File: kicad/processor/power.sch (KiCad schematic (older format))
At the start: 29 parts, among them J201 V_QI, J202 GND, J301 Battery, Q203 DMG3415U, Q204 DMG3415U, Q301 DMG3414U, Q302 DMG3415U, Q303 DMG3415U, U301 MCP73832, U302 NCP694-3.3

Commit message: Restructure directories - separate projects for each board,
separate directory for analysis, datasheets
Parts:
- removed LED301: Charge, paddle:SMD_D_0805, symbol LED3MM
- added LED?: LED, paddle:SMD_D_0805, symbol LED
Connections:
- wire segments 72 -> 96
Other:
- moved on the sheet: D?

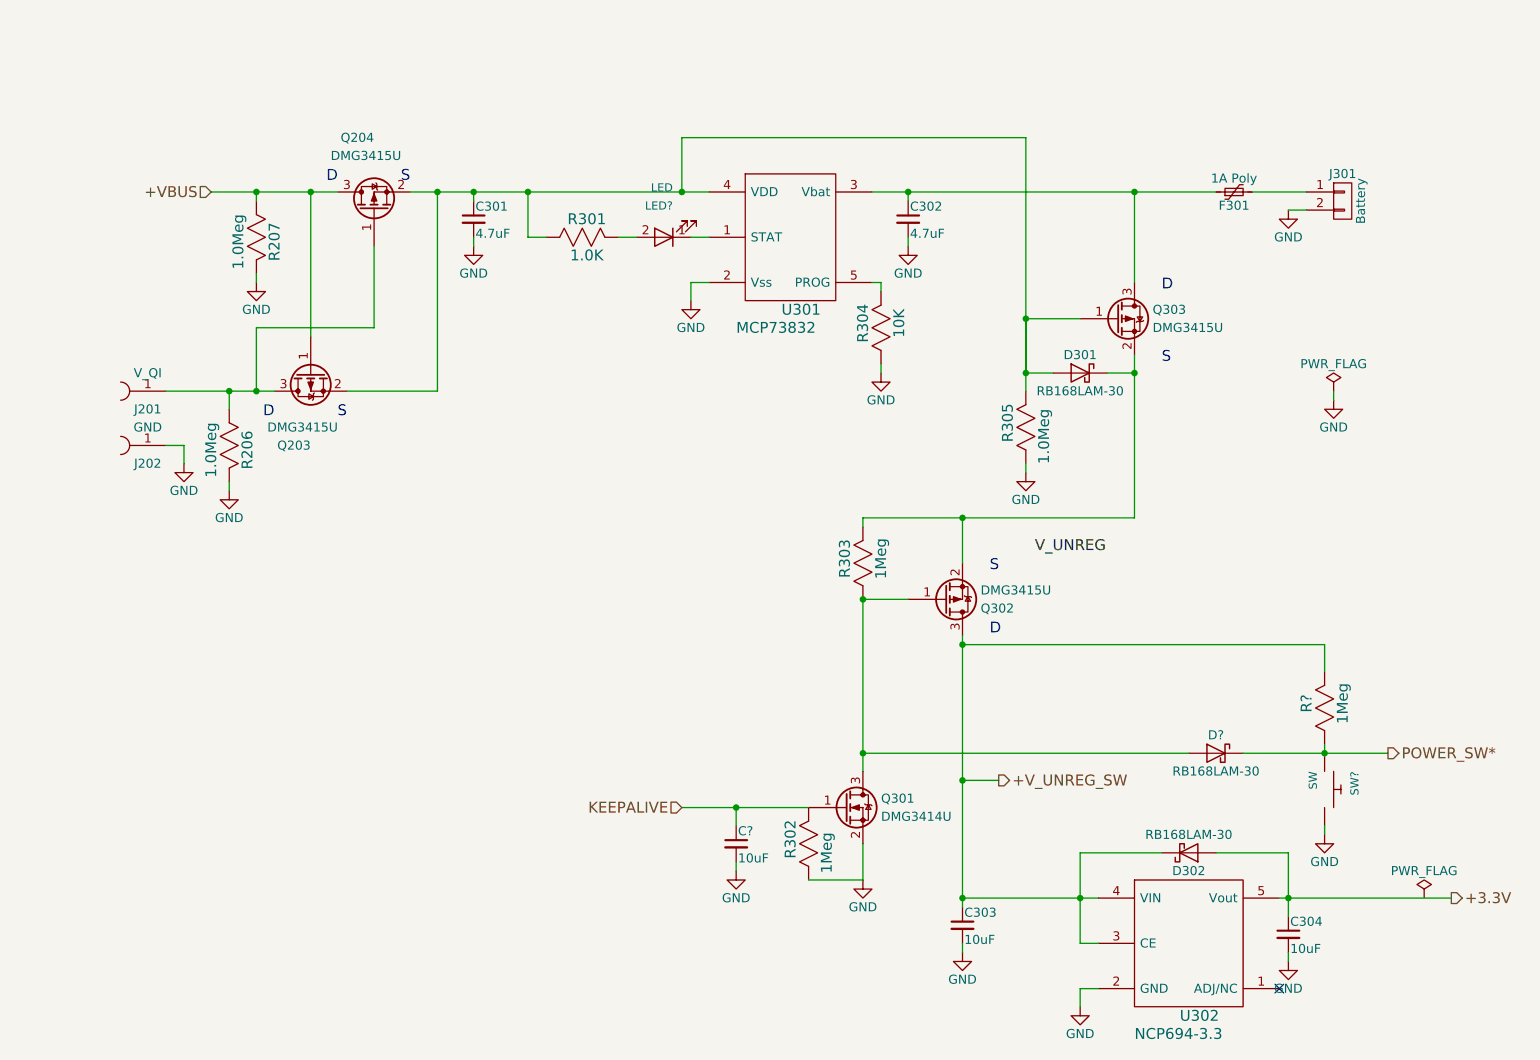
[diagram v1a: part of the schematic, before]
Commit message: Finish split projects, fix ERC, import outline to processor board
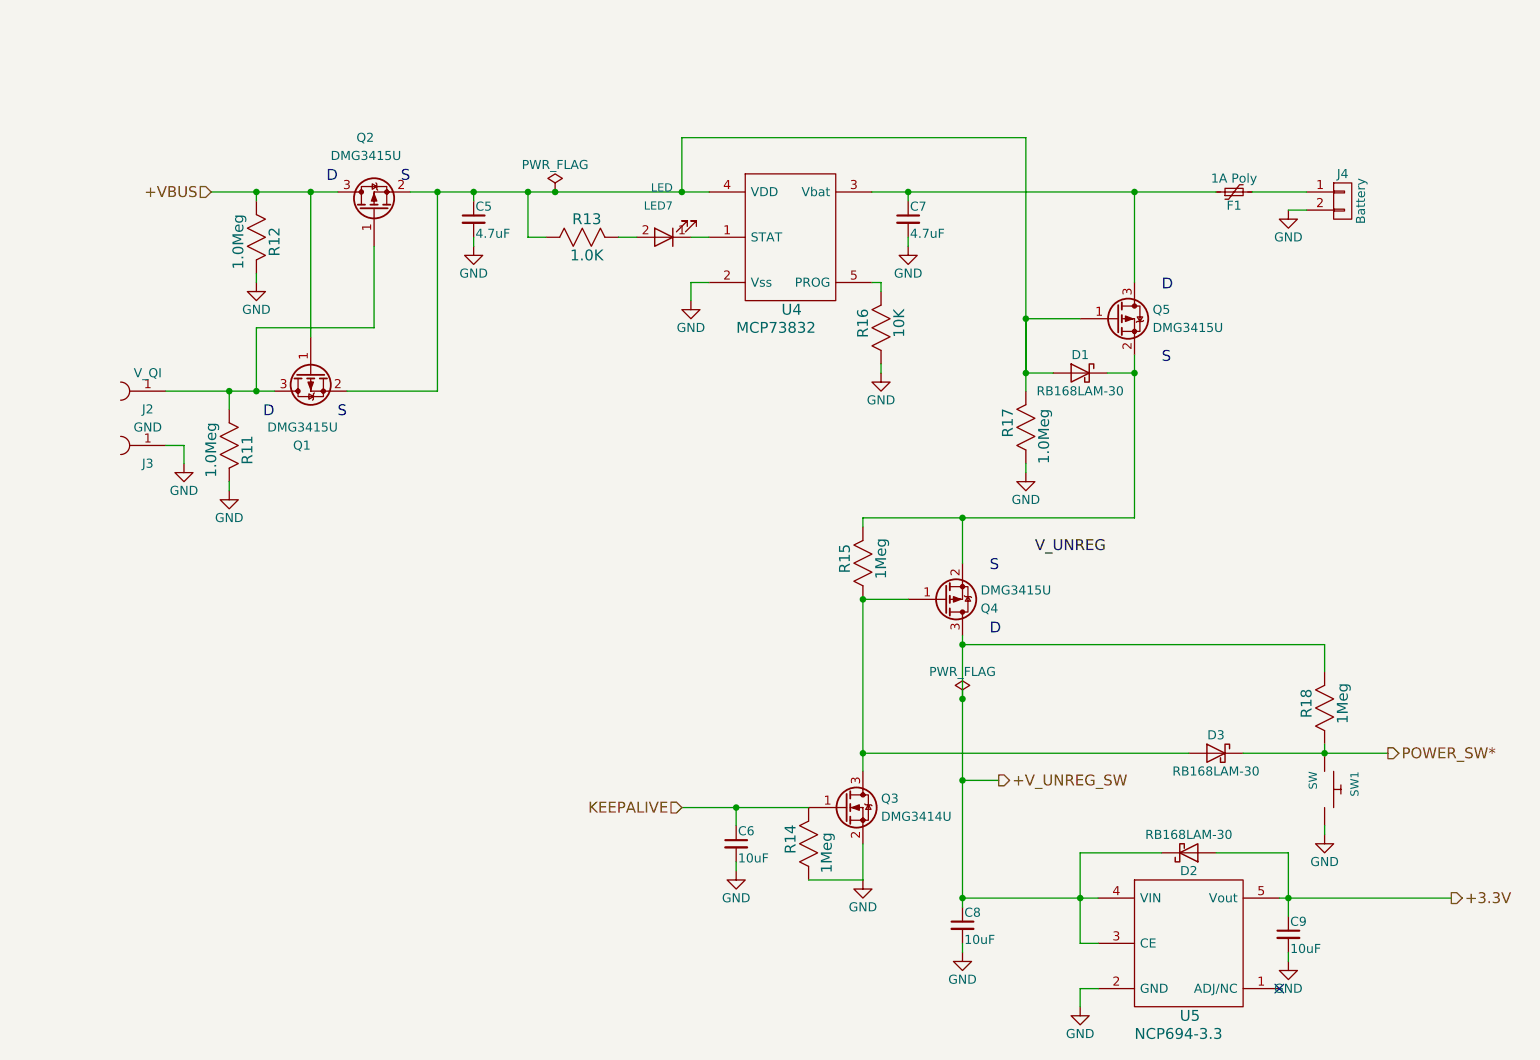
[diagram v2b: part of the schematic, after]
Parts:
- gave numbers to parts that had none: 5
- renumbered C301 to C5, C302 to C7, C303 to C8, C304 to C9, D301 to D1, D302 to D2, F301 to F1, J201 to J2, J202 to J3, J301 to J4, Q203 to Q1, Q204 to Q2, Q301 to Q3, Q302 to Q4, Q303 to Q5, R206 to R11, R207 to R12, R301 to R13, R302 to R14, R303 to R15, R304 to R16, R305 to R17, U301 to U4, U302 to U5

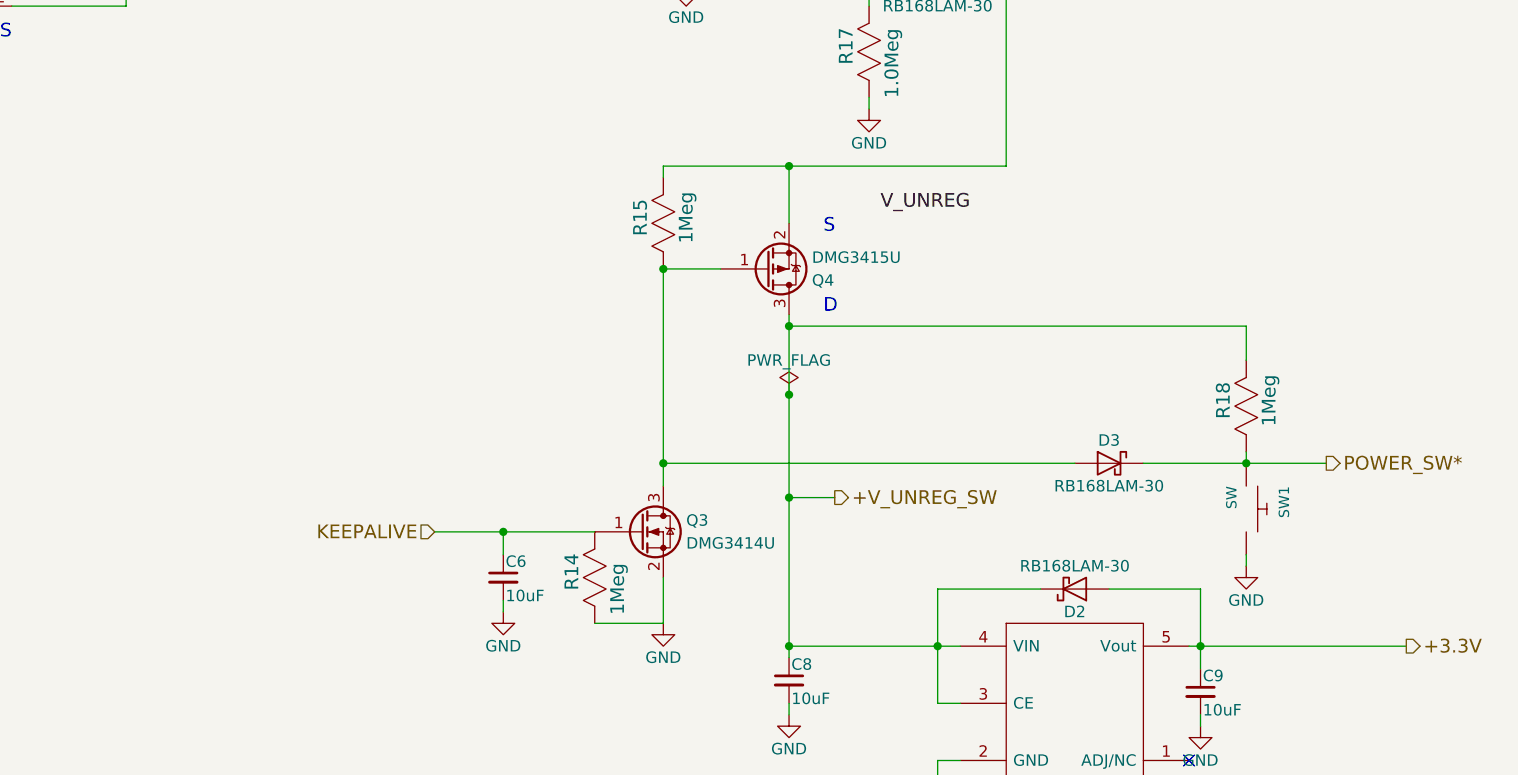
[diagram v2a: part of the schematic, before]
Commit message: Logic board standalone about done, changed to 0603 resistors and 0805 caps
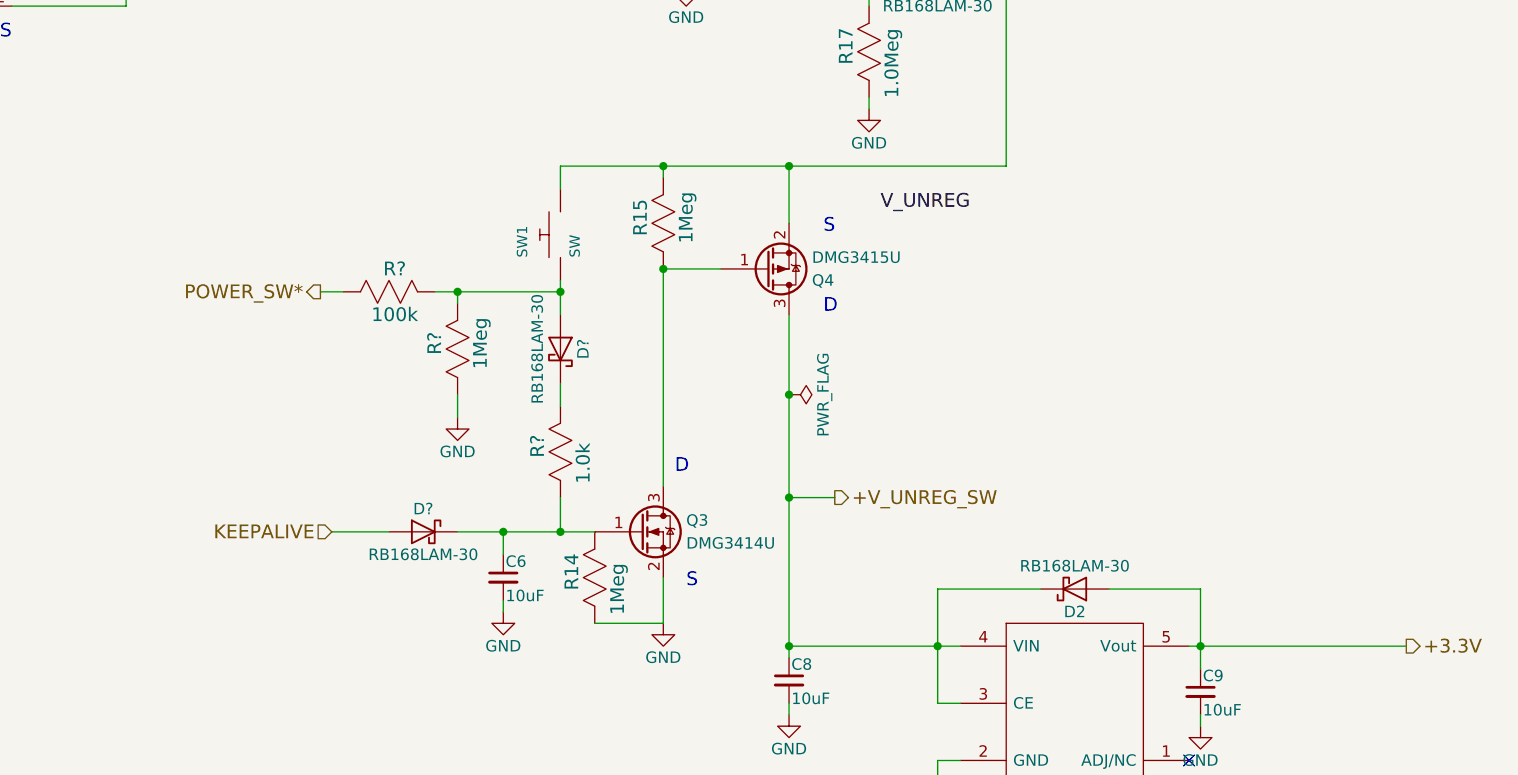
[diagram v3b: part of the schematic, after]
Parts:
- removed D3: RB168LAM-30, paddle:D_SOD-123, symbol Schottky
- removed R18: 1Meg, paddle:SMD_0805, symbol R_US
- added D? (x2): RB168LAM-30, paddle:D_SOD-128, symbol Schottky
- added R?: 1.0k, paddle:R_0603, symbol R_US
- added R?: 1Meg, paddle:R_0603, symbol R_US
- added R?: 100k, paddle:R_0603, symbol R_US
- C5, C6, C7, C8, C9: footprint paddle:SMD_1206 -> paddle:SMD_0805
- D1: footprint paddle:D_SOD-123 -> paddle:D_SOD-128
- R11, R12, R13, R14, R15, R16, R17: footprint paddle:SMD_0805 -> paddle:R_0603
- SW1: footprint paddle:SW_TACTILE_PB_SMD_6MM -> paddle:SW_KMR7
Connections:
- net GND: now also R?.1; no longer SW1.2
- net KEEPALIVE: now also D?.1; no longer C6.1, Q3.1 (G), R14.2
- net POWER_SW*: now also R?.1; no longer SW1.1
- net at D1.2, Q4.2 (S), Q5.2 (S)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: now also SW1.2
- new net: C6.1, D?.2, Q3.1 (G), R14.2, R?.1
- new net: D?.1, R?.2, R?.2, SW1.1
- new net: D?.2, R?.2
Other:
- moved on the sheet: SW1
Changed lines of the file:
@@
 F 0 "C8" H 6710 5970 50  0000 L CNN
 F 1 "10uF" H 6710 5820 50  0000 L CNN
-F 2 "paddle:SMD_1206" H 6700 5900 50  0001 C CNN
+F 2 "paddle:SMD_0805" H 6700 5900 50  0001 C CNN
 F 3 "" H 6700 5900 50  0001 C CNN
 	1    6700 5900
@@
 F 0 "R15" H 6175 4000 60  0000 C CNN
 F 1 "1Meg" H 6175 3800 60  0000 C CNN
-F 2 "paddle:SMD_0805" H 6150 3550 60  0001 C CNN
+F 2 "paddle:R_0603" H 6150 3550 60  0001 C CNN
 F 3 "" H 6175 4000 60  0000 C CNN
 	1    6150 3900
@@
 F 0 "R14" H 5875 5550 60  0000 C CNN
 F 1 "1Meg" H 5800 5350 60  0000 C CNN
-F 2 "paddle:SMD_0805" H 5850 5100 60  0001 C CNN
+F 2 "paddle:R_0603" H 5850 5100 60  0001 C CNN
 F 3 "" H 5875 5550 60  0000 C CNN
 	1    5850 5450
@@
 F 0 "C5" H 4010 2070 50  0000 L CNN
 F 1 "4.7uF" H 4010 1920 50  0000 L CNN
-F 2 "paddle:SMD_1206" H 4000 2000 50  0001 C CNN
+F 2 "paddle:SMD_0805" H 4000 2000 50  0001 C CNN
 F 3 "" H 4000 2000 50  0001 C CNN
 	1    4000 2000
@@
 F 0 "R16" H 6275 2700 60  0000 C CNN
 F 1 "10K" H 6275 2500 60  0000 C CNN
-F 2 "paddle:SMD_0805" H 6250 2250 60  0001 C CNN
+F 2 "paddle:R_0603" H 6250 2250 60  0001 C CNN
 F 3 "" H 6275 2700 60  0000 C CNN
 	1    6250 2600
@@
 	1    0    0    -1
 $EndComp
-Text HLabel 9050 4950 2    60   Output ~ 0
+Text HLabel 4650 4200 0    60   Output ~ 0
 POWER_SW*
-Text HLabel 5150 5250 0    60   Input ~ 0
+Text HLabel 4700 5250 0    60   Input ~ 0
 KEEPALIVE
 $Comp
@@
 F 0 "C7" H 6410 2070 50  0000 L CNN
 F 1 "4.7uF" H 6410 1920 50  0000 L CNN
-F 2 "paddle:SMD_1206" H 6400 2000 50  0001 C CNN
+F 2 "paddle:SMD_0805" H 6400 2000 50  0001 C CNN
 F 3 "" H 6400 2000 50  0001 C CNN
 	1    6400 2000
@@
 F 0 "R13" H 4625 2200 60  0000 C CNN
 F 1 "1.0K" H 4625 2000 60  0000 C CNN
-F 2 "paddle:SMD_0805" H 4600 1750 60  0001 C CNN
+F 2 "paddle:R_0603" H 4600 1750 60  0001 C CNN
 F 3 "" H 4625 2200 60  0000 C CNN
 	1    4600 2100
@@
 F 0 "C9" H 8510 6020 50  0000 L CNN
 F 1 "10uF" H 8510 5870 50  0000 L CNN
-F 2 "paddle:SMD_1206" H 8500 5950 50  0001 C CNN
+F 2 "paddle:SMD_0805" H 8500 5950 50  0001 C CNN
 F 3 "" H 8500 5950 50  0001 C CNN
 	1    8500 5950
@@
 F 0 "R17" H 7075 3250 60  0000 C CNN
 F 1 "1.0Meg" H 7000 3050 60  0000 C CNN
-F 2 "paddle:SMD_0805" H 7050 2800 60  0001 C CNN
+F 2 "paddle:R_0603" H 7050 2800 60  0001 C CNN
 F 3 "" H 7075 3250 60  0000 C CNN
 	1    7050 3150
@@
 F 0 "D1" H 7350 2950 50  0000 C CNN
 F 1 "RB168LAM-30" H 7350 2750 50  0000 C CNN
-F 2 "paddle:D_SOD-123" H 7350 2675 50  0001 C CNN
+F 2 "paddle:D_SOD-128" H 7350 2675 50  0001 C CNN
 F 3 "" H 7350 2850 50  0001 C CNN
 	1    7350 2850
@@
 L GND #PWR039
 U 1 1 59D182BE
-P 8700 5400
-F 0 "#PWR039" H 8700 5150 50  0001 C CNN
-F 1 "GND" H 8700 5250 50  0000 C CNN
-F 2 "" H 8700 5400 50  0001 C CNN
-F 3 "" H 8700 5400 50  0001 C CNN
-	1    8700 5400
+P 5250 4750
+F 0 "#PWR039" H 5250 4500 50  0001 C CNN
+F 1 "GND" H 5250 4600 50  0000 C CNN
+F 2 "" H 5250 4750 50  0001 C CNN
+F 3 "" H 5250 4750 50  0001 C CNN
+	1    5250 4750
 	1    0    0    -1
 $EndComp
@@
 F 0 "R11" H 2675 3350 60  0000 C CNN
 F 1 "1.0Meg" H 2675 3150 60  0000 C CNN
-F 2 "paddle:SMD_0805" H 2650 2900 60  0001 C CNN
+F 2 "paddle:R_0603" H 2650 2900 60  0001 C CNN
 F 3 "" H 2675 3350 60  0000 C CNN
 	1    2650 3250
@@
 F 0 "R12" H 2825 2200 60  0000 C CNN
 F 1 "1.0Meg" H 2825 2000 60  0000 C CNN
-F 2 "paddle:SMD_0805" H 2800 1750 60  0001 C CNN
+F 2 "paddle:R_0603" H 2800 1750 60  0001 C CNN
 F 3 "" H 2825 2200 60  0000 C CNN
 	1    2800 2100
@@
 	1    0    0    -1
 $EndComp
-$Comp
-L Schottky D3
-U 1 1 59F6B4CB
-P 8100 4950
-F 0 "D3" H 8100 5050 50  0000 C CNN
-F 1 "RB168LAM-30" H 8100 4850 50  0000 C CNN
-F 2 "paddle:D_SOD-123" H 8100 4775 50  0001 C CNN
-F 3 "" H 8100 4950 50  0001 C CNN
-	1    8100 4950
-	1    0    0    -1
-$EndComp
 Wire Wire Line
 	6700 6000 6700 6050
@@
 	6150 4100 6400 4100
 Wire Wire Line
-	5150 5250 5850 5250
+	5250 5250 5850 5250
 Wire Wire Line
 	6150 5450 6150 5650
@@
 Connection ~ 2800 2950
 Wire Wire Line
-	8700 4900 8700 4950
-Wire Wire Line
-	8250 4950 9050 4950
-Wire Wire Line
-	6150 3650 7650 3650
-Wire Wire Line
 	6700 3650 6700 3900
 Connection ~ 6700 3650
 Wire Wire Line
 	7650 3650 7650 2750
-Wire Wire Line
-	6700 4350 8700 4350
-Wire Wire Line
-	8700 4350 8700 4500
-Connection ~ 6700 4350
-Wire Wire Line
-	7950 4950 6150 4950
-Connection ~ 6150 4950
-$Comp
-L R_US R18
-U 1 1 59F6B547
-P 8700 4700
-F 0 "R18" H 8725 4800 60  0000 C CNN
-F 1 "1Meg" H 8725 4600 60  0000 C CNN
-F 2 "paddle:SMD_0805" H 8700 4350 60  0001 C CNN
-F 3 "" H 8725 4800 60  0000 C CNN
-	1    8700 4700
-	0    -1   -1   0
-$EndComp
 $Comp
 L SWITCH_PUSHBUTTON SW?
 U 1 1 59F6C3BE
-P 8700 5150
+P 5700 3950
 AR Path="/59B548AE/59F6C3BE" Ref="SW?"  Part="1"
 AR Path="/59FE1414/59FE32E0/59F6C3BE" Ref="SW?"  Part="1"
 AR Path="/59FFABEE/59F6C3BE" Ref="SW1"  Part="1"
-F 0 "SW1" H 8600 5290 45  0000 L BNN
-F 1 "SW" H 8600 5060 45  0000 L BNN
-F 2 "paddle:SW_TACTILE_PB_SMD_6MM" H 9000 5350 20  0001 C CNN
-F 3 "" H 8700 5150 60  0001 C CNN
-	1    8700 5150
-	0    1    1    0
-$EndComp
-Wire Wire Line
-	8700 5350 8700 5400
-Connection ~ 8700 4950
+F 0 "SW1" H 5600 4090 45  0000 L BNN
+F 1 "SW" H 5600 3860 45  0000 L BNN
+F 2 "paddle:SW_KMR7" H 6000 4150 20  0001 C CNN
+F 3 "" H 5700 3950 60  0001 C CNN
+	1    5700 3950
+	0    -1   -1   0
+$EndComp
 Wire Wire Line
 	5150 1850 5150 1550
@@
 F 0 "C6" H 5460 5520 50  0000 L CNN
 F 1 "10uF" H 5460 5370 50  0000 L CNN
-F 2 "paddle:SMD_1206" H 5450 5450 50  0001 C CNN
+F 2 "paddle:SMD_0805" H 5450 5450 50  0001 C CNN
 F 3 "" H 5450 5450 50  0001 C CNN
 	1    5450 5450
@@
 F 3 "" H 6700 4650 50  0001 C CNN
 	1    6700 4650
-	1    0    0    -1
+	0    1    1    0
 $EndComp
 Connection ~ 6700 4650
 Connection ~ 4450 1850
+$Comp
+L Schottky D?
+U 1 1 5A0BC7B3
+P 5700 4450
+F 0 "D?" H 5700 4550 50  0000 C CNN
+F 1 "RB168LAM-30" H 5700 4350 50  0000 C CNN
+F 2 "paddle:D_SOD-128" H 5700 4275 50  0001 C CNN
+F 3 "" H 5700 4450 50  0001 C CNN
+	1    5700 4450
+	0    1    1    0
+$EndComp
+$Comp
+L Schottky D?
+U 1 1 5A0BC847
+P 5100 5250
+F 0 "D?" H 5100 5350 50  0000 C CNN
+F 1 "RB168LAM-30" H 5100 5150 50  0000 C CNN
+F 2 "paddle:D_SOD-128" H 5100 5075 50  0001 C CNN
+F 3 "" H 5100 5250 50  0001 C CNN
+	1    5100 5250
+	1    0    0    -1
+$EndComp
+Wire Wire Line
+	4950 5250 4700 5250
+Connection ~ 5700 5250
+Wire Wire Line
+	5700 4150 5700 4300
+Wire Wire Line
+	5700 3750 5700 3650
+Connection ~ 6150 3650
+$Comp
+L R_US R?
+U 1 1 5A0BD110
+P 5700 4900
+F 0 "R?" H 5725 5000 60  0000 C CNN
+F 1 "1.0k" H 5650 4800 60  0000 C CNN
+F 2 "paddle:R_0603" H 5700 4550 60  0001 C CNN
+F 3 "" H 5725 5000 60  0000 C CNN
+	1    5700 4900
+	0    -1   -1   0
+$EndComp
+Wire Wire Line
+	5700 4600 5700 4700
+Wire Wire Line
+	5700 5100 5700 5250
+$Comp
+L R_US R?
+U 1 1 5A0BD777
+P 5250 4450
+F 0 "R?" H 5275 4550 60  0000 C CNN
+F 1 "1Meg" H 5275 4350 60  0000 C CNN
+F 2 "paddle:R_0603" H 5250 4100 60  0001 C CNN
+F 3 "" H 5275 4550 60  0000 C CNN
+	1    5250 4450
+	0    -1   -1   0
+$EndComp
+Wire Wire Line
+	5150 4200 5700 4200
+Wire Wire Line
+	5250 4200 5250 4250
+Connection ~ 5700 4200
+Wire Wire Line
+	5250 4650 5250 4750
+Connection ~ 5250 4200
+Wire Wire Line
+	5700 3650 7650 3650
+$Comp
+L R_US R?
+U 1 1 5A0BE1FB
+P 4950 4200
+F 0 "R?" H 4975 4300 60  0000 C CNN
+F 1 "100k" H 4975 4100 60  0000 C CNN
+F 2 "paddle:R_0603" H 4950 3850 60  0001 C CNN
+F 3 "" H 4975 4300 60  0000 C CNN
+	1    4950 4200
+	1    0    0    -1
+$EndComp
+Wire Wire Line
+	4750 4200 4650 4200
+Text Notes 6250 5500 0    60   ~ 0
+S
+Text Notes 6200 5000 0    60   ~ 0
+D
 $EndSCHEMATC
